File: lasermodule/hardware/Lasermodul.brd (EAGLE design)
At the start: 51.7 x 35.5 mm, 79 parts, among them IC1 MEGA8-AI

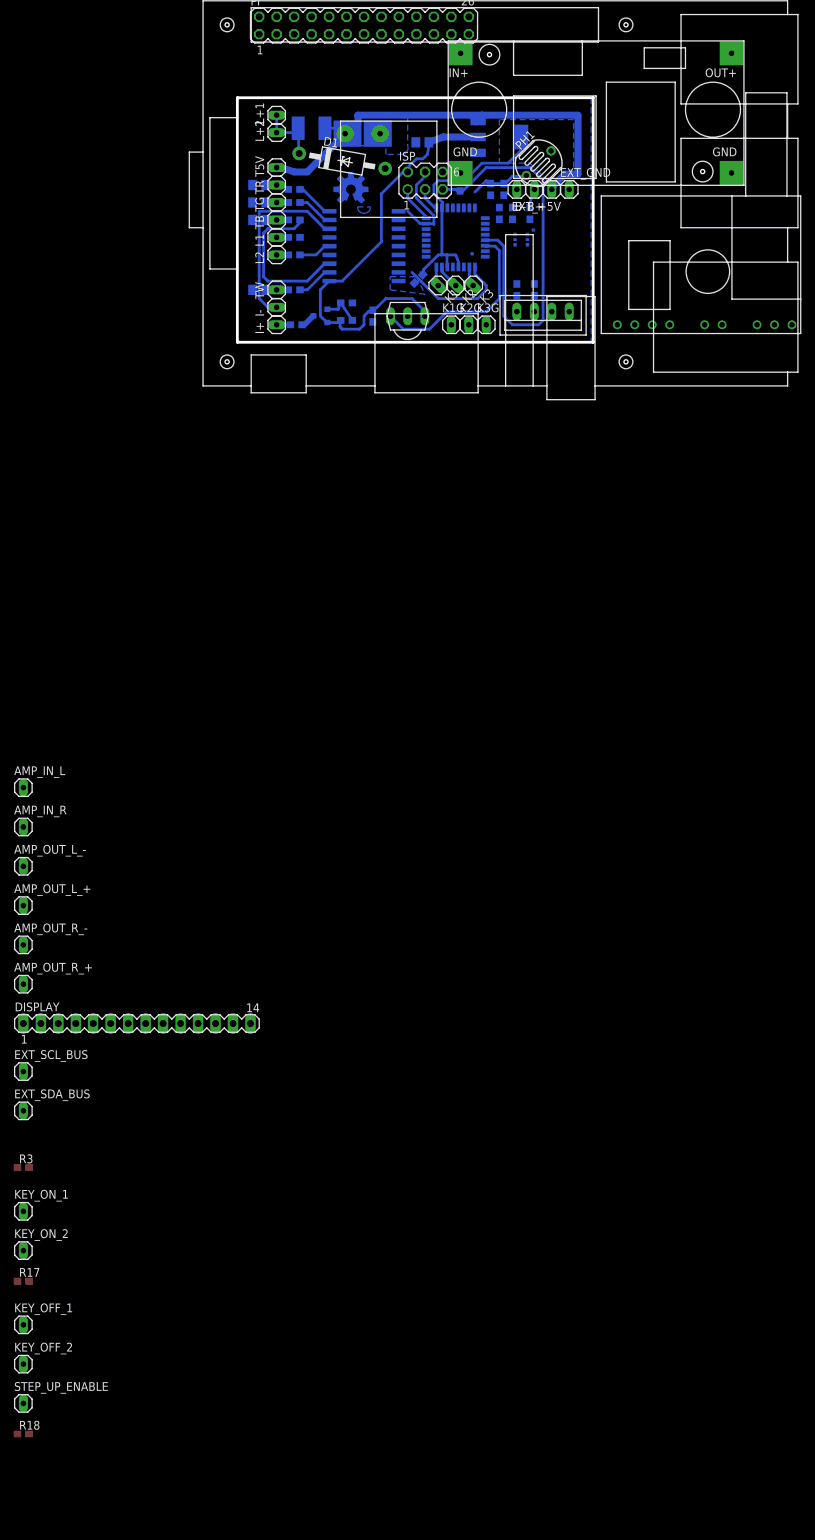
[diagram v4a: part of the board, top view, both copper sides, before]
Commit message: lasermodul schaltplan rc1
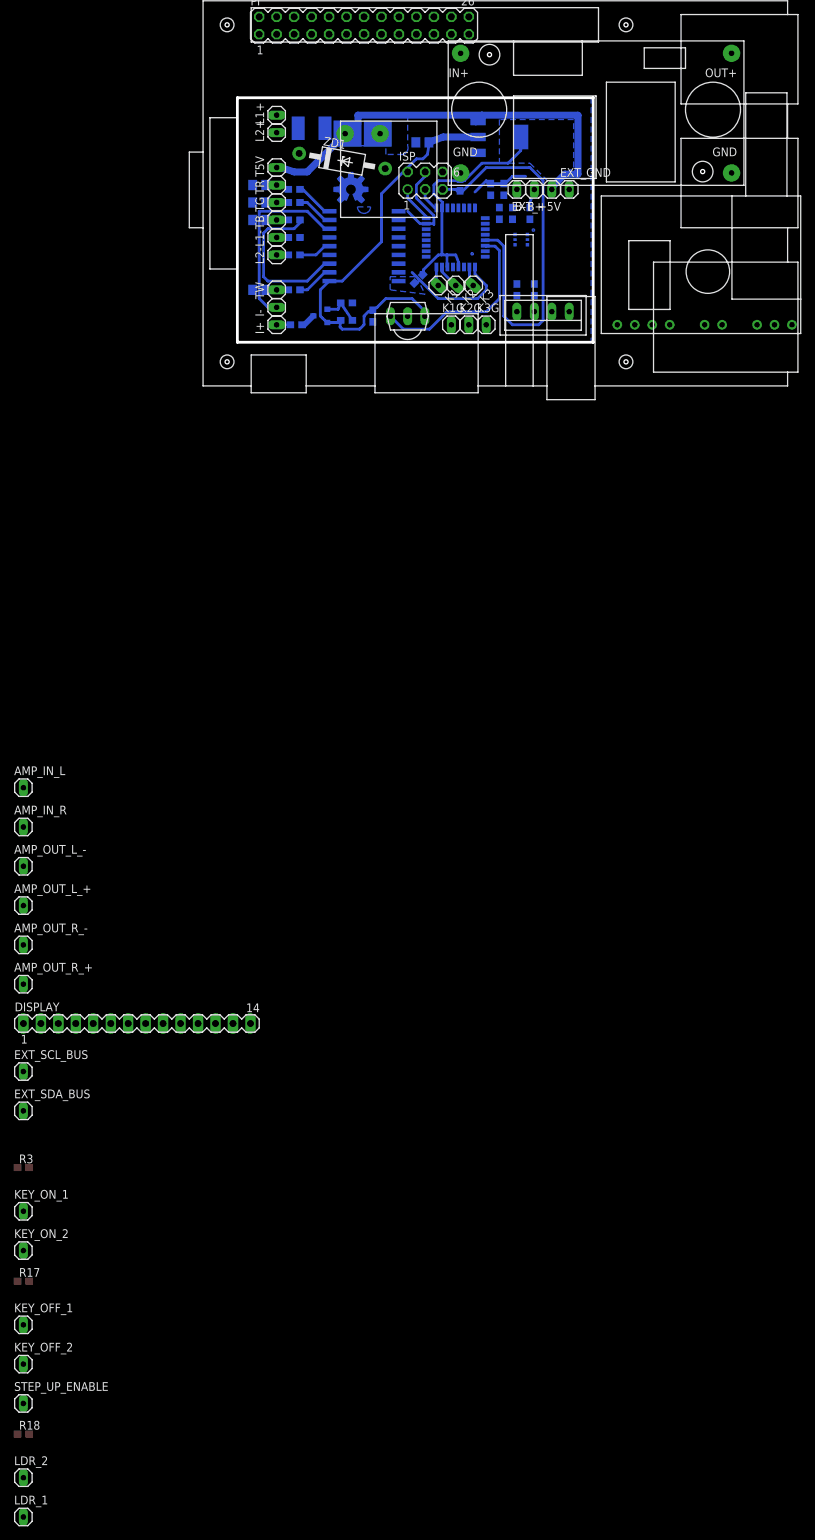
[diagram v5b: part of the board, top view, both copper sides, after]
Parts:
- removed PH1: VT80N1, photo-elements:VT800
- added LDR_1, LDR_2: (no value), wz:PIN-HEADER-1
- renumbered D1 to ZD1, L+1 to L1+, L+2 to L2+, L1 to L1-, L2 to L2-
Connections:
- removed net LASER_+: FUSE.2, L1+.1, L2+.1, ZD1.C
- new net N$28: FUSE.1, U$3.OUT+
- net +3V3: now also LDR_1.1; no longer PH1.1
- net +5V: now also FUSE.2, L1+.1, L2+.1, ZD1.C; no longer FUSE.1, U$3.OUT+
- net AMBI_LIGHT: now also LDR_2.1; no longer PH1.2
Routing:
- net LASER_+: track 10.4 -> 0.00 mm
- net +5V: track 72.1 -> 69.0 mm
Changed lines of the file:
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@@
 </element>
 <element name="R13" library="wz" package="0603" value="10k" x="32.385" y="22.86" rot="MR270"/>
-<element name="D1" library="wz" package="Z-DIODE" value="5,6V" x="15.24" y="26.3525" rot="R350"/>
-<element name="L2" library="wz" package="PIN-HEADER-1" value="" x="5.715" y="12.7" rot="R90"/>
-<element name="L1" library="wz" package="PIN-HEADER-1" value="" x="5.715" y="15.24" rot="R90"/>
-<element name="L+1" library="wz" package="PIN-HEADER-1" value="" x="5.715" y="33.02" rot="R90"/>
-<element name="L+2" library="wz" package="PIN-HEADER-1" value="" x="5.715" y="30.48" rot="R90"/>
+<element name="ZD1" library="wz" package="Z-DIODE" value="5,6V" x="15.24" y="26.3525" rot="R350"/>
+<element name="L2-" library="wz" package="PIN-HEADER-1" value="" x="5.715" y="12.7" rot="R90"/>
+<element name="L1-" library="wz" package="PIN-HEADER-1" value="" x="5.715" y="15.24" rot="R90"/>
+<element name="L1+" library="wz" package="PIN-HEADER-1" value="" x="5.715" y="33.02" rot="R90"/>
+<element name="L2+" library="wz" package="PIN-HEADER-1" value="" x="5.715" y="30.48" rot="R90"/>
 <element name="TG" library="wz" package="PIN-HEADER-1" value="" x="5.715" y="20.32" rot="R90"/>
 <element name="TR" library="wz" package="PIN-HEADER-1" value="" x="5.715" y="22.86" rot="R90"/>
@@
 <element name="K2G" library="wz" package="PIN-HEADER-1" value="" x="33.655" y="2.54"/>
 <element name="K3G" library="wz" package="PIN-HEADER-1" value="" x="36.195" y="2.54"/>
-<element name="PH1" library="photo-elements" package="VT800" value="VT80N1" x="43.815" y="26.035" rot="R225"/>
 <element name="R16" library="wz" package="0603" value="10k" x="38.735" y="22.225" rot="MR90"/>
 <element name="C4" library="wz" package="0603" value="100n" x="36.83" y="22.225" rot="MR270"/>
@@
 <element name="STEP_UP_ENABLE" library="wz" package="PIN-HEADER-1" value="" x="-31.115" y="-154.305"/>
 <element name="R18" library="wz" package="0603" value="10k" x="-31.115" y="-158.75"/>
+<element name="LDR_2" library="wz" package="PIN-HEADER-1" value="" x="-31.115" y="-165.1"/>
+<element name="LDR_1" library="wz" package="PIN-HEADER-1" value="" x="-31.115" y="-170.815"/>
 </elements>
 <signals>
 <signal name="+5V">
 <contactref element="T5V" pad="1"/>
-<contactref element="FUSE" pad="1"/>
 <contactref element="EXT_+5V" pad="1"/>
 <contactref element="LM1117" pad="3"/>
 <contactref element="C3" pad="1"/>
-<wire x1="12.745" y1="31.115" x2="12.7" y2="31.75" width="0.4064" layer="16"/>
 <wire x1="5.715" y1="25.4" x2="6.35" y2="25.4" width="1.016" layer="16"/>
 <wire x1="6.35" y1="25.4" x2="8.255" y2="24.765" width="1.016" layer="16"/>
@@
 <wire x1="16.011" y1="30.33" x2="15.725" y2="30.33" width="0.4064" layer="16"/>
 <wire x1="15.725" y1="30.33" x2="14.605" y2="29.21" width="0.4064" layer="16"/>
-<wire x1="12.745" y1="31.115" x2="15.226" y2="31.115" width="0.4064" layer="16"/>
 <wire x1="15.226" y1="31.115" x2="16.011" y2="30.33" width="0.4064" layer="16"/>
 <contactref element="BUS" pad="P$2"/>
 <contactref element="C3" pad="1B"/>
-<contactref element="U$3" pad="OUT+"/>
 <contactref element="U$4" pad="VCC"/>
 <contactref element="PI" pad="2"/>
 <contactref element="PI" pad="4"/>
-<wire x1="49.53" y1="33.02" x2="71.86" y2="42.015" width="0" layer="19" extent="16-16"/>
+<contactref element="L1+" pad="1"/>
+<contactref element="L2+" pad="1"/>
+<contactref element="FUSE" pad="2"/>
+<contactref element="ZD1" pad="C"/>
+<wire x1="45.72" y1="4.445" x2="70.485" y2="2.54" width="0" layer="19" extent="1-1"/>
+<wire x1="45.72" y1="22.225" x2="45.72" y2="4.445" width="0" layer="19" extent="1-1"/>
 <wire x1="15.675" y1="30.33" x2="15.725" y2="30.33" width="0" layer="19" extent="16-16"/>
-<wire x1="5.715" y1="47.325" x2="12.7" y2="31.75" width="0" layer="19" extent="16-16"/>
+<wire x1="8.98646875" y1="27.455165625" x2="8.255" y2="24.765" width="0" layer="19" extent="16-16"/>
+<wire x1="8.845" y1="31.115" x2="8.98646875" y2="27.455165625" width="0" layer="19" extent="16-16"/>
+<wire x1="5.715" y1="30.48" x2="8.845" y2="31.115" width="0" layer="19" extent="16-16"/>
+<wire x1="5.715" y1="33.02" x2="5.715" y2="30.48" width="0" layer="19" extent="1-1"/>
+<wire x1="5.715" y1="47.325" x2="5.715" y2="33.02" width="0" layer="19" extent="1-1"/>
 <wire x1="3.175" y1="47.325" x2="5.715" y2="47.325" width="0" layer="19" extent="1-1"/>
-<wire x1="45.72" y1="4.445" x2="45.72" y2="22.225" width="0" layer="19" extent="1-1"/>
-<wire x1="70.485" y1="2.54" x2="45.72" y2="4.445" width="0" layer="19" extent="1-1"/>
 </signal>
 <signal name="GND">
@@
 <contactref element="C2" pad="2"/>
 <contactref element="D2" pad="2"/>
-<contactref element="D1" pad="A"/>
 <contactref element="EXT_GND" pad="1"/>
 <contactref element="U$1" pad="GND"/>
@@
 <contactref element="R3" pad="2"/>
 <contactref element="B-" pad="1"/>
+<contactref element="ZD1" pad="A"/>
 <wire x1="-30.265" y1="-120.015" x2="-31.115" y2="-148.59" width="0" layer="19" extent="1-1"/>
 <wire x1="2.225" y1="7.62" x2="-30.265" y2="-120.015" width="0" layer="19" extent="1-16"/>
@@
 <wire x1="3.81" y1="15.875" x2="3.81" y2="9.525" width="0.4064" layer="16"/>
 <wire x1="3.81" y1="9.525" x2="4.445" y2="8.89" width="0.4064" layer="16"/>
-</signal>
-<signal name="LASER_+">
-<contactref element="L+2" pad="1"/>
-<contactref element="L+1" pad="1"/>
-<contactref element="FUSE" pad="2"/>
-<contactref element="D1" pad="C"/>
-<wire x1="8.845" y1="31.115" x2="9.525" y2="30.48" width="0.4064" layer="16"/>
-<wire x1="5.715" y1="30.48" x2="5.715" y2="33.02" width="0.4064" layer="16"/>
-<wire x1="8.845" y1="31.115" x2="8.845" y2="30.525" width="0.4064" layer="16"/>
-<wire x1="8.845" y1="30.525" x2="8.89" y2="30.48" width="0.4064" layer="16"/>
-<wire x1="8.89" y1="30.48" x2="5.715" y2="30.48" width="0.4064" layer="16"/>
-<wire x1="8.98646875" y1="27.455165625" x2="8.89" y2="27.455165625" width="0.4064" layer="16"/>
-<wire x1="8.89" y1="27.455165625" x2="8.89" y2="30.48" width="0.4064" layer="16"/>
 </signal>
 <signal name="IR_TAKT_-">
@@
 <wire x1="27.6225" y1="27.305" x2="27.94" y2="29.015" width="0.4064" layer="16"/>
 <wire x1="27.94" y1="29.015" x2="27.855" y2="29.06" width="0.4064" layer="16"/>
-<contactref element="PH1" pad="1"/>
 <wire x1="26.95354375" y1="9.808540625" x2="26.89686875" y2="9.93313125" width="0.4064" layer="16"/>
 <wire x1="26.89686875" y1="9.93313125" x2="26.67" y2="10.16" width="0.4064" layer="16"/>
@@
 <wire x1="29.655" y1="12.7" x2="29.75" y2="12.795" width="0.4064" layer="16"/>
 <wire x1="30.48" y1="12.7" x2="29.655" y2="12.7" width="0.4064" layer="16"/>
+<contactref element="LDR_1" pad="1"/>
+<wire x1="15.24" y1="1.905" x2="-31.115" y2="-170.815" width="0" layer="19" extent="16-16"/>
 <wire x1="26.95354375" y1="9.808540625" x2="25.4" y2="6.35" width="0" layer="19" extent="16-16"/>
 </signal>
 <signal name="N$12">
-<contactref element="L1" pad="1"/>
+<contactref element="L1-" pad="1"/>
 <contactref element="R1" pad="2"/>
 <wire x1="5.715" y1="15.24" x2="7.405" y2="15.24" width="0.4064" layer="16"/>
@@
 <signal name="N$18">
 <contactref element="R2" pad="2"/>
-<contactref element="L2" pad="1"/>
+<contactref element="L2-" pad="1"/>
 <wire x1="7.405" y1="12.7" x2="5.715" y2="12.7" width="0.4064" layer="16"/>
 </signal>
@@
 <signal name="AMBI_LIGHT">
 <contactref element="IC1" pad="24"/>
-<contactref element="PH1" pad="2"/>
 <contactref element="R16" pad="2"/>
 <contactref element="C4" pad="1"/>
@@
 <wire x1="39.05" y1="23.175" x2="40.005" y2="24.13" width="0.4064" layer="16"/>
 <wire x1="40.005" y1="24.13" x2="41.91" y2="24.13" width="0.4064" layer="16"/>
-<wire x1="41.91" y1="24.13" x2="42.018946875" y2="24.238946875" width="0.4064" layer="16"/>
 <wire x1="34.55" y1="21.85" x2="36.195" y2="23.495" width="0.4064" layer="16"/>
-<wire x1="34.55" y1="19.5326" x2="34.55" y2="21.85" width="0" layer="19" extent="16-16"/>
+<contactref element="LDR_2" pad="1"/>
+<wire x1="34.55" y1="19.5326" x2="-31.115" y2="-165.1" width="0" layer="19" extent="16-16"/>
+<wire x1="34.55" y1="21.85" x2="34.55" y2="19.5326" width="0" layer="19" extent="16-16"/>
 </signal>
 <signal name="TX">
@@
 <wire x1="-31.115" y1="-126.365" x2="-31.965" y2="-136.525" width="0" layer="19" extent="1-1"/>
 </signal>
+<signal name="N$28">
+<contactref element="U$3" pad="OUT+"/>
+<contactref element="FUSE" pad="1"/>
+<wire x1="12.745" y1="31.115" x2="71.86" y2="42.015" width="0" layer="19" extent="16-16"/>
+</signal>
 </signals>

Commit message: started plexi tiefzieh case
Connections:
- new net STEPUP_EN: KEY_OFF_1.1, R17.2, R18.2, R3.1, STEP_UP_ENABLE.1
- net ONOFF: no longer KEY_OFF_1.1, R17.2, R18.2, R3.1, STEP_UP_ENABLE.1
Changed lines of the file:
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@@
 <signal name="ONOFF">
 <contactref element="IC1" pad="32"/>
-<contactref element="R3" pad="1"/>
-<contactref element="R17" pad="2"/>
-<contactref element="KEY_OFF_1" pad="1"/>
-<contactref element="STEP_UP_ENABLE" pad="1"/>
-<contactref element="R18" pad="2"/>
 <contactref element="R18" pad="1"/>
-<wire x1="-30.265" y1="-158.75" x2="-31.965" y2="-158.75" width="0" layer="19" extent="1-1"/>
-<wire x1="-31.115" y1="-154.305" x2="-31.965" y2="-158.75" width="0" layer="19" extent="1-1"/>
-<wire x1="-31.115" y1="-142.875" x2="-31.115" y2="-154.305" width="0" layer="19" extent="1-1"/>
-<wire x1="-30.265" y1="-136.525" x2="-31.115" y2="-142.875" width="0" layer="19" extent="1-1"/>
-<wire x1="-31.965" y1="-120.015" x2="-30.265" y2="-136.525" width="0" layer="19" extent="1-1"/>
-<wire x1="36.0426" y1="12.44" x2="-31.965" y2="-120.015" width="0" layer="19" extent="1-16"/>
+<wire x1="36.0426" y1="12.44" x2="-31.965" y2="-158.75" width="0" layer="19" extent="1-16"/>
 </signal>
 <signal name="N$26">
@@
 <wire x1="12.745" y1="31.115" x2="71.86" y2="42.015" width="0" layer="19" extent="16-16"/>
 </signal>
+<signal name="STEPUP_EN">
+<contactref element="STEP_UP_ENABLE" pad="1"/>
+<contactref element="R17" pad="2"/>
+<contactref element="R18" pad="2"/>
+<contactref element="R3" pad="1"/>
+<contactref element="KEY_OFF_1" pad="1"/>
+<wire x1="-31.115" y1="-154.305" x2="-30.265" y2="-158.75" width="0" layer="19" extent="1-1"/>
+<wire x1="-31.115" y1="-142.875" x2="-31.115" y2="-154.305" width="0" layer="19" extent="1-1"/>
+<wire x1="-30.265" y1="-136.525" x2="-31.115" y2="-142.875" width="0" layer="19" extent="1-1"/>
+<wire x1="-31.965" y1="-120.015" x2="-30.265" y2="-136.525" width="0" layer="19" extent="1-1"/>
+</signal>
 </signals>

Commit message: lasermodul: second ir led added (shotgun, sniper)
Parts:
- removed R9: 10, wz:0603
- added IR_-_1, IR_SHOTGUN_+: (no value), wz:PIN-HEADER-1
- added P-FET2, P-FET3: (no value), zetex:SOT-23
- added R19, R21, R22, R24: 10, wz:0603
- added R20, R23: 10k, wz:0603
- renumbered B+ to BATT+, B- to BATT-, I+ to IR_SNIPER_+, I- to IR_-_2, K1 to KEY1, K1G to KEY1G, K2 to KEY2, K2G to KEY2G, K3 to KEY3, K3G to KEY3G, P-FET to P-FET1
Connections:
- removed net IR_TX_+: IR_SNIPER_+.1, R9.1
- removed net N$16: P-FET1.1, R9.2
- new net +3V2: P-FET1.1, P-FET2.2, P-FET3.2, R20.2, R23.2
- new net IR_SHORGUN_TX_+: IR_SHOTGUN_+.1, R24.1
- new net IR_SNIPER_TX_+: IR_SNIPER_+.1, R21.1
- new net I_IR_SHOTGUN: IC1.26, R22.1
- new net I_IR_SNIPER: IC1.23, R19.1
- new net N$34: P-FET2.1, R21.2
- new net N$46: P-FET2.3, R19.2, R20.1
- new net N$53: P-FET3.1, R24.2
- new net N$54: P-FET3.3, R22.2, R23.1
- net IR_TAKT_-: now also IR_-_1.1
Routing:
- net N$16: track 2.18 -> 0.00 mm
- net IR_TX_+: track 1.99 -> 0.00 mm

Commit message: Revert "lasermodul: second ir led added (shotgun, sniper)"
This reverts commit 9edbfcc3dcd4b30951dc51917cfd3b2c003d7d33.
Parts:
- removed IR_-_1, IR_SHOTGUN_+: (no value), wz:PIN-HEADER-1
- removed P-FET2, P-FET3: (no value), zetex:SOT-23
- removed R19, R21, R22, R24: 10, wz:0603
- removed R20, R23: 10k, wz:0603
- added R9: 10, wz:0603
- renumbered BATT+ to B+, BATT- to B-, IR_-_2 to I-, IR_SNIPER_+ to I+, KEY1 to K1, KEY1G to K1G, KEY2 to K2, KEY2G to K2G, KEY3 to K3, KEY3G to K3G, P-FET1 to P-FET
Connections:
- removed net +3V2: P-FET.1, P-FET2.2, P-FET3.2, R20.2, R23.2
- removed net IR_SHORGUN_TX_+: IR_SHOTGUN_+.1, R24.1
- removed net IR_SNIPER_TX_+: I+.1, R21.1
- removed net I_IR_SHOTGUN: IC1.26, R22.1
- removed net I_IR_SNIPER: IC1.23, R19.1
- removed net N$34: P-FET2.1, R21.2
- removed net N$46: P-FET2.3, R19.2, R20.1
- removed net N$53: P-FET3.1, R24.2
- removed net N$54: P-FET3.3, R22.2, R23.1
- new net IR_TX_+: I+.1, R9.1
- new net N$16: P-FET.1, R9.2
- net IR_TAKT_-: no longer IR_-_1.1
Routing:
- net N$16: track 0.00 -> 2.18 mm
- net IR_TX_+: track 0.00 -> 1.99 mm
